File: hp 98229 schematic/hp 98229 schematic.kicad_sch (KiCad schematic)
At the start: 109 parts, among them J1 Conn_02x36_Top_Bottom, U10 74AHCT04, U11 74AHCT04, U21 74AHCT04, U22 74AHCT04, U41 74AHCT04

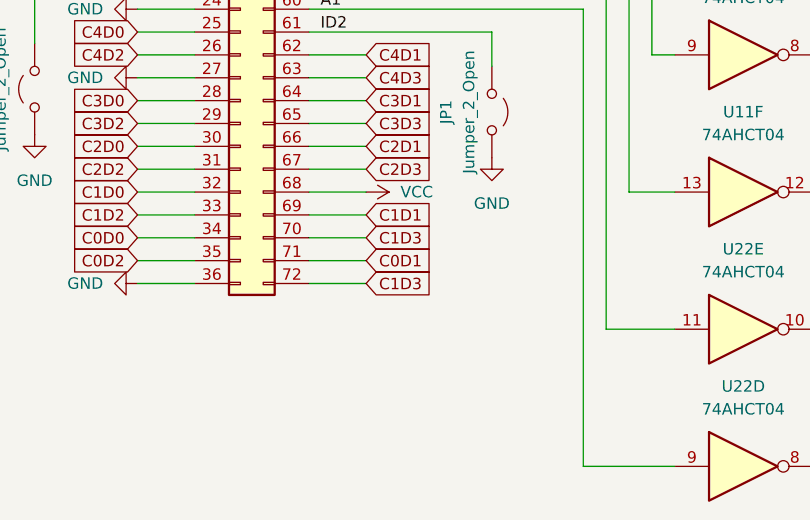
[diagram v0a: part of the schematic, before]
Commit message: fix C0D3 label on connector
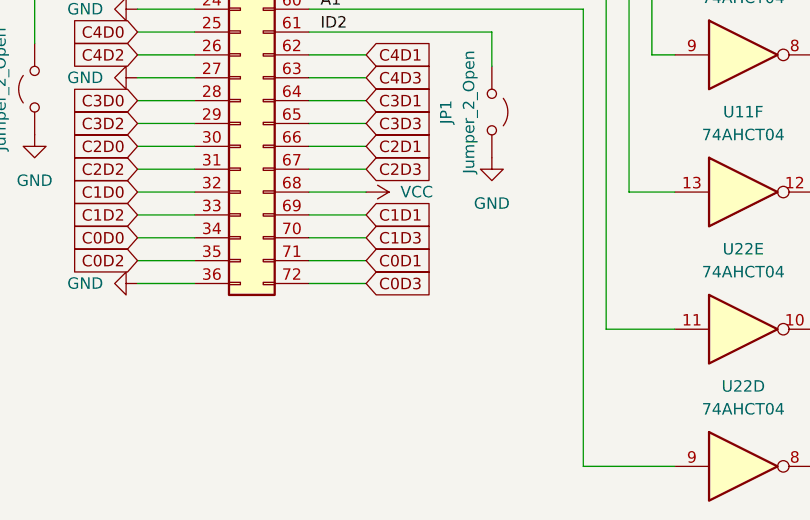
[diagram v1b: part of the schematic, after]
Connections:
- net C0D3: now also J1.72 (Pin_72)
- net C1D3: no longer J1.72 (Pin_72)
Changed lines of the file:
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@@
 		)
 	)
-	(global_label "C1D3"
+	(global_label "C0D3"
 		(shape input)
 		(at 273.05 379.73 0)

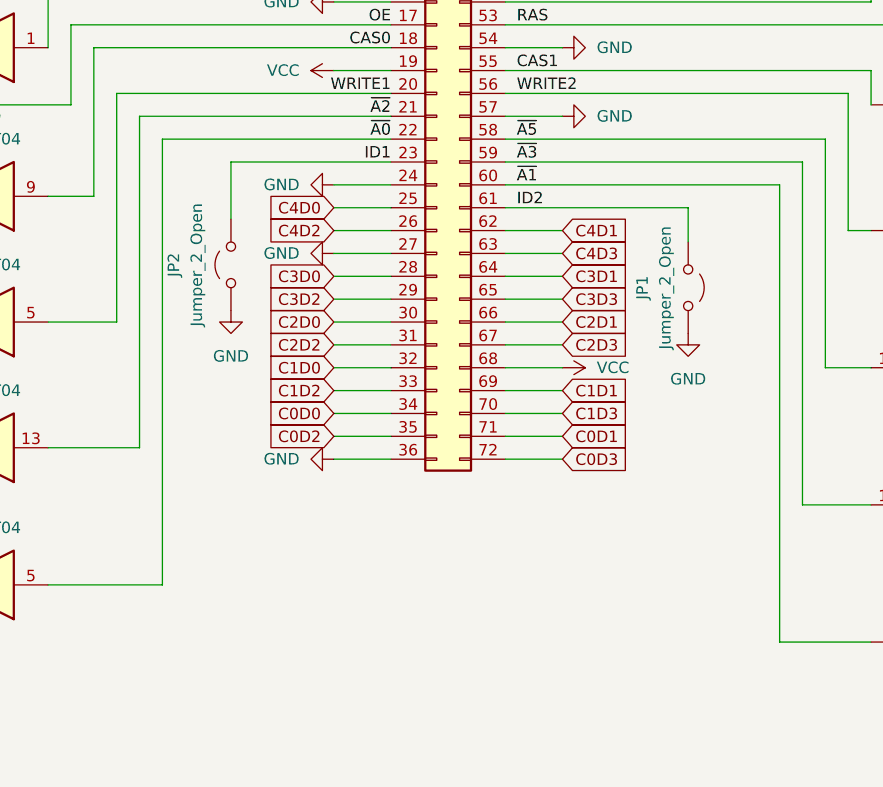
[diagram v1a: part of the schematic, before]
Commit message: Add table to show id jumper configurations
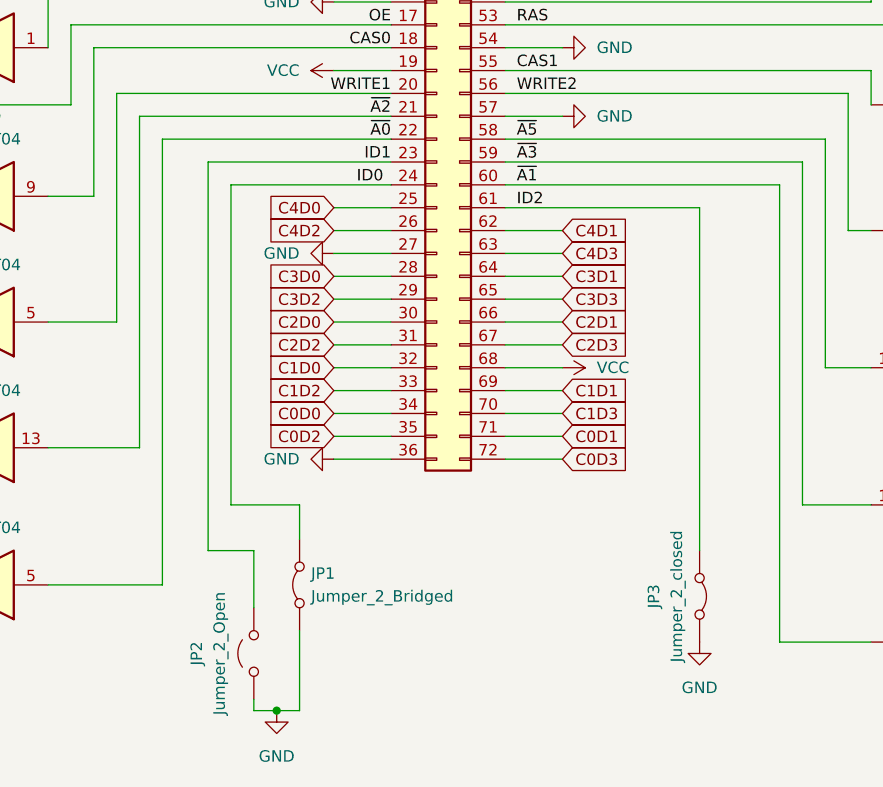
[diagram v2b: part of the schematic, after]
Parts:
- added JP1: Jumper_2_Bridged, Jumper:SolderJumper-2_P1.3mm_Bridged_RoundedPad1.0x1.5mm, symbol Jumper:Jumper_2_Bridged
- C1, C10, C11, C12, C13, C14, C15, C16, C17, C18, C19, C2, C20, C21, C22, C23, C24, C25, C26, C27, C28, C29, C3, C30, C31, C32, C33, C34, C35, C36, C37, C38, C39, C4, C5, C6, C7, C8, C9: footprint (none) -> Capacitor_SMD:C_1210_3225Metric_Pad1.33x2.70mm_HandSolder
- C50: footprint (none) -> Capacitor_Tantalum_SMD:CP_EIA-7343-20_Kemet-V_Pad2.25x2.55mm_HandSolder
- J1: footprint (none) -> Connector_PinSocket_2.54mm:PinSocket_2x36_P2.54mm_Horizontal
- JP2: footprint (none) -> Jumper:SolderJumper-2_P1.3mm_Open_RoundedPad1.0x1.5mm
- JP3: renamed from JP1; value Jumper_2_Open -> Jumper_2_closed; footprint (none) -> Jumper:SolderJumper-2_P1.3mm_Bridged_RoundedPad1.0x1.5mm; symbol Jumper:Jumper_2_Open -> Jumper:Jumper_2_Bridged
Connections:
- net GND: now also JP1.1 (A); no longer J1.24 (Pin_24)
- new net ID0: J1.24 (Pin_24), JP1.2 (B)
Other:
- moved on the sheet: JP2, JP3
